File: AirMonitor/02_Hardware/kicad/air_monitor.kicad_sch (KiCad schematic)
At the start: 1 part, among them U1 ESP32-WROVER-B

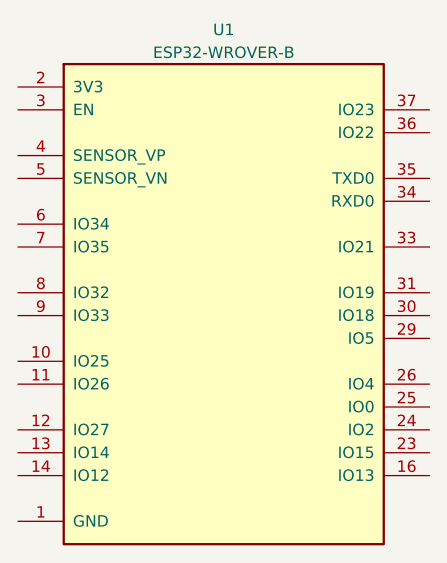
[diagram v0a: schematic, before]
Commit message: Update MCU identification to STM32F407ZGT6 and generate STIST PBL project report
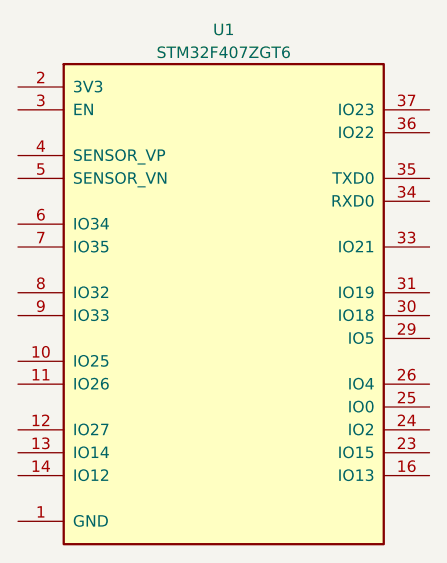
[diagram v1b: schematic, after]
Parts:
- U1: value ESP32-WROVER-B -> STM32F407ZGT6; footprint RF_Module:ESP32-WROVER-B -> Package_QFP:LQFP-144_20x20mm_P0.5mm; symbol RF_Module:ESP32-WROVER-B -> MCU_ST_STM32F4:STM32F407ZGTx
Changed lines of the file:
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@@
 		(rev "1.0")
 		(company "Air Monitor Engineering Team")
-		(comment 1 "Core MCU: Espressif ESP32-WROVER-B")
+		(comment 1 "Core MCU: STMicroelectronics STM32F407ZGT6 (LQFP-144)")
 		(comment 2 "Environmental Sensing & UI Subsystems")
 		(comment 3 "Power Domain: 1S Li-Ion / USB Type-C 5V")
 	)
-	(symbol (lib_id "RF_Module:ESP32-WROVER-B") (at 175.26 124.46 0) (unit 1)
+	(symbol (lib_id "MCU_ST_STM32F4:STM32F407ZGTx") (at 175.26 124.46 0) (unit 1)
 		(in_bom yes) (on_board yes) (dnp no)
 		(property "Reference" "U1" (at 175.26 93.98 0) (effects (font (size 1.27 1.27))))
-		(property "Value" "ESP32-WROVER-B" (at 175.26 96.52 0) (effects (font (size 1.27 1.27))))
-		(property "Footprint" "RF_Module:ESP32-WROVER-B" (at 175.26 124.46 0) (effects (font (size 1.27 1.27)) hide))
-		(property "Datasheet" "https://www.espressif.com" (at 175.26 124.46 0) (effects (font (size 1.27 1.27)) hide))
+		(property "Value" "STM32F407ZGT6" (at 175.26 96.52 0) (effects (font (size 1.27 1.27))))
+		(property "Footprint" "Package_QFP:LQFP-144_20x20mm_P0.5mm" (at 175.26 124.46 0) (effects (font (size 1.27 1.27)) hide))
+		(property "Datasheet" "https://www.st.com/resource/en/datasheet/stm32f407zg.pdf" (at 175.26 124.46 0) (effects (font (size 1.27 1.27)) hide))
 		(pin "1")
 		(pin "2")
